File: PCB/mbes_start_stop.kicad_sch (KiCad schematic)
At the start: 15 parts, among them J1 IXTP3N50D2, Q10 BC817, Q12 BC817, Q16 BC817, Q17 BC327, Q18 BC327

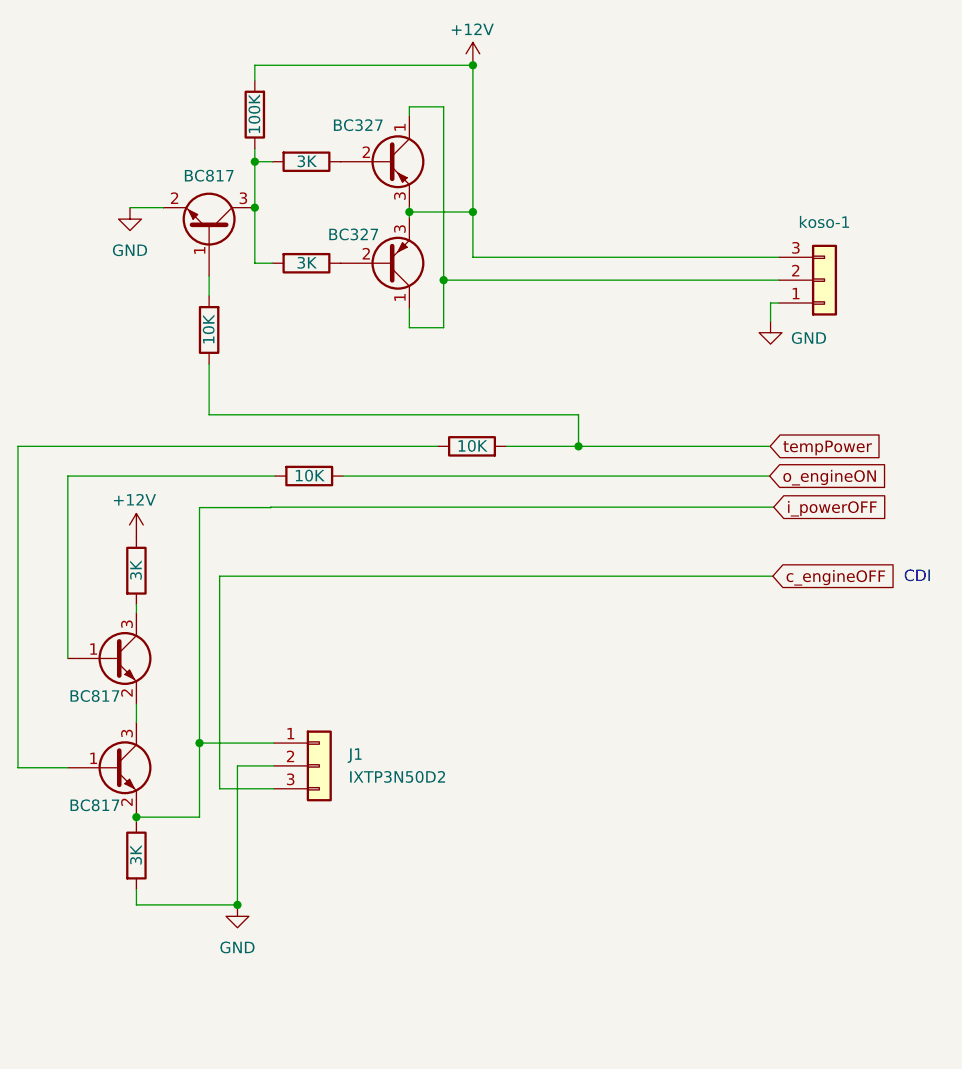
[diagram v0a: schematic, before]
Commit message: Engine-off mechanism
Deplation MOSfet has been substituted by a mechanical relay
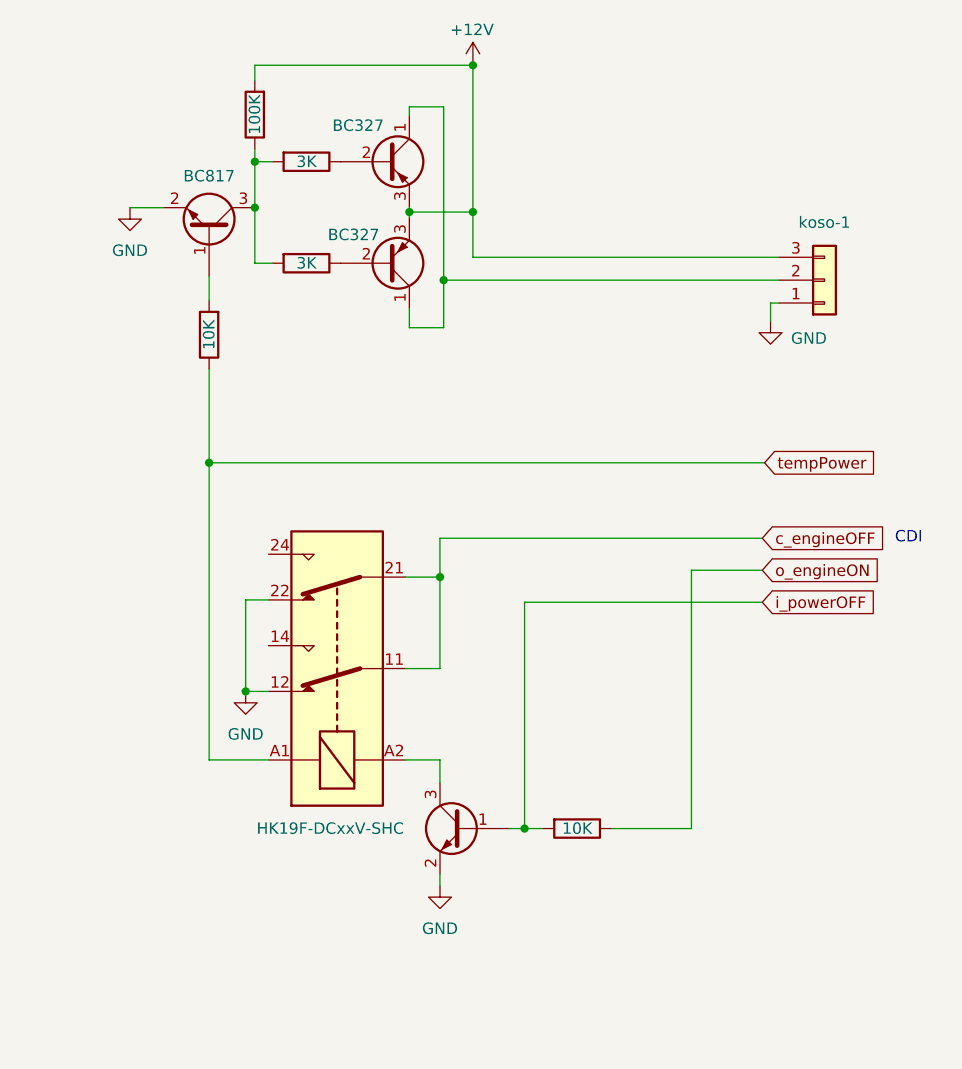
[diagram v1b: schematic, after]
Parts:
- removed J1: IXTP3N50D2, Connector_PinHeader_1.27mm:PinHeader_1x03_P1.27mm_Horizontal, symbol Connector_Generic:Conn_01x03
- removed Q16: BC817, Package_TO_SOT_SMD:SOT-23, symbol Transistor_BJT:BC817
- removed RA23: 10K, Resistor_SMD:R_1206_3216Metric, symbol Device:R
- removed RA29, RA43: 3K, Resistor_SMD:R_1206_3216Metric, symbol Device:R
- added K1: HK19F-DCxxV-SHC, Relay_THT:Relay_DPDT_Finder_30.22, symbol Relay:HK19F-DCxxV-SHC
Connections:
- net GND: now also Q12.2 (E), K1.12, K1.22
- net c_engineOFF: now also K1.11, K1.21
- net i_powerOFF: now also Q12.1 (B), RA44.2; no longer Q12.2 (E)
- net tempPower: now also K1.A1
- net at Q12.3 (C): now also K1.A2

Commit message: Wrong relay's power supply fixed
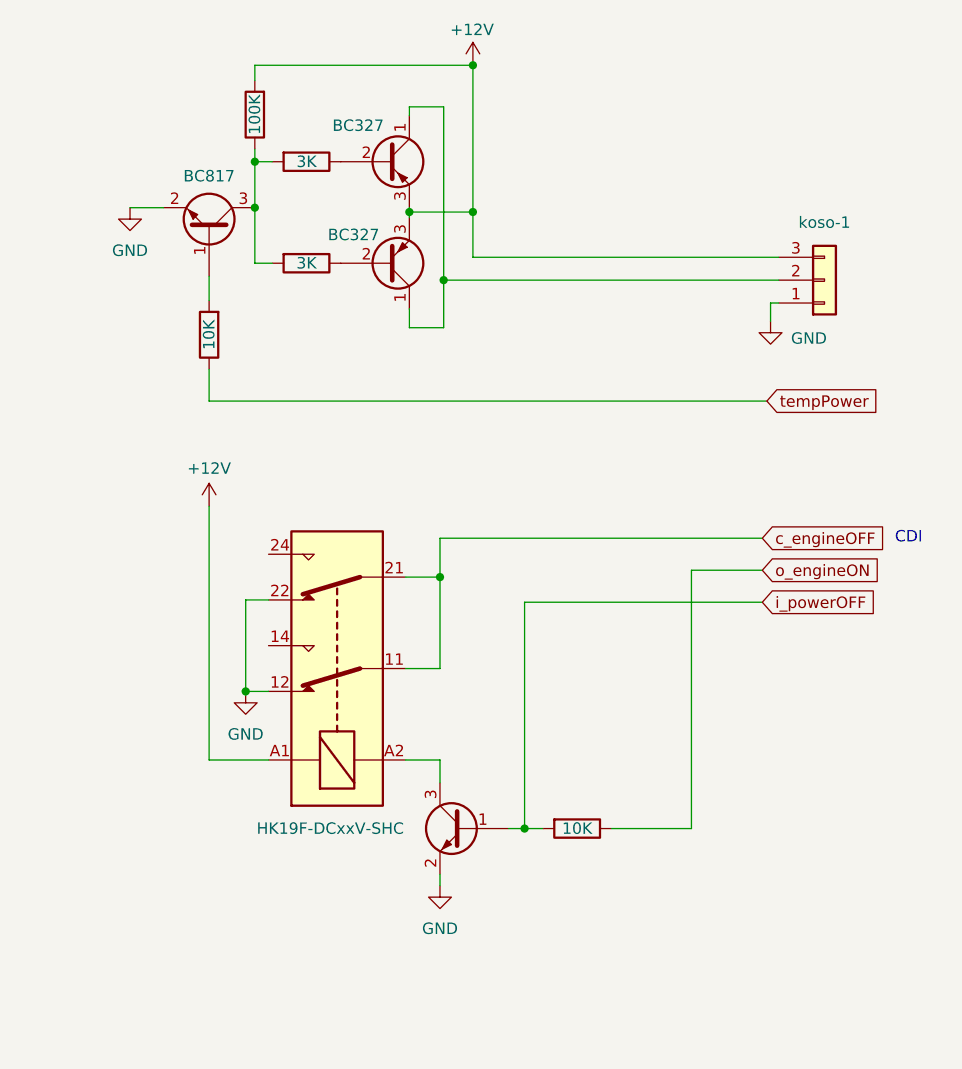
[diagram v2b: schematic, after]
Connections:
- net +12V: now also K1.A1
- net tempPower: no longer K1.A1
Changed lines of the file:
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@@
-	)
-	(junction
-		(at 89.916 121.92)
-		(diameter 0)
-		(color 0 0 0 0)
 	)
 	(junction
@@
 	(wire
 		(pts
-			(xy 89.916 111.506) (xy 89.916 121.92)
+			(xy 89.916 111.506) (xy 89.916 115.062)
 		)
 		(stroke
@@
 	(wire
 		(pts
+			(xy 89.916 126.746) (xy 89.916 154.94)
+		)
+		(stroke
+			(width 0)
+			(type default)
+		)
+	)
+	(wire
+		(pts
 			(xy 112.1664 94.0562) (xy 119.2276 94.0562)
 		)
@@
 	(wire
 		(pts
-			(xy 151.638 121.92) (xy 89.916 121.92)
+			(xy 151.892 115.062) (xy 89.916 115.062)
 		)
 		(stroke
@@
 		(pts
 			(xy 111.76 134.62) (xy 115.57 134.62)
-		)
-		(stroke
-			(width 0)
-			(type default)
-		)
-	)
-	(wire
-		(pts
-			(xy 89.916 121.92) (xy 89.916 154.94)
 		)
 		(stroke
@@
 	(global_label "tempPower"
 		(shape input)
-		(at 151.638 121.92 0)
+		(at 151.892 115.062 0)
 		(fields_autoplaced yes)
 		(effects
@@
 		)
 		(property "Intersheetrefs" "${INTERSHEET_REFS}"
-			(at 151.638 121.92 0)
+			(at 151.892 115.062 0)
 			(effects
 				(font
@@
 		)
 		(property "Riferimenti inter-foglio" "${INTERSHEET_REFS}"
-			(at 164.3321 121.8406 0)
+			(at 164.5861 114.9826 0)
 			(effects
 				(font
@@
 					(unit 1)
 				)
+			)
+		)
+	)
+	(symbol
+		(lib_id "power:+12V")
+		(at 89.916 126.746 0)
+		(unit 1)
+		(exclude_from_sim no)
+		(in_bom yes)
+		(on_board yes)
+		(dnp no)
+		(property "Reference" "#PWR04"
+			(at 89.916 130.556 0)
+			(effects
+				(font
+					(size 1.27 1.27)
+				)
+				(hide yes)
+			)
+		)
+		(property "Value" "+12V"
+			(at 89.916 122.555 0)
+			(effects
+				(font
+					(size 1.27 1.27)
+				)
+			)
+		)
+		(property "Footprint" ""
+			(at 89.916 126.746 0)
+			(effects
+				(font
+					(size 1.27 1.27)
+				)
+				(hide yes)
+			)
+		)
+		(property "Datasheet" ""
+			(at 89.916 126.746 0)
+			(effects
+				(font
+					(size 1.27 1.27)
+				)
+				(hide yes)
+			)
+		)
+		(property "Description" ""
+			(at 89.916 126.746 0)
+			(effects
+				(font
+					(size 1.27 1.27)
+				)
+				(hide yes)
+			)
+		)
+		(pin "1"
+		)
+		(instances
+			(project "pcb-b"
+				(path "/709d0967-afe5-49d3-92a5-d2bb94550bdb/58129762-4641-4cf0-a39a-a6f0d215df4c"
+					(reference "#PWR04")
+					(unit 1)
+				)

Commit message: More stable solution for BJT driving
The BJT-817 device's sensibility is very high. If you are doing some test and you weld a wire to che i_PowerOFF pin, then you
can find the transistor's sturation while the wire is not connected.
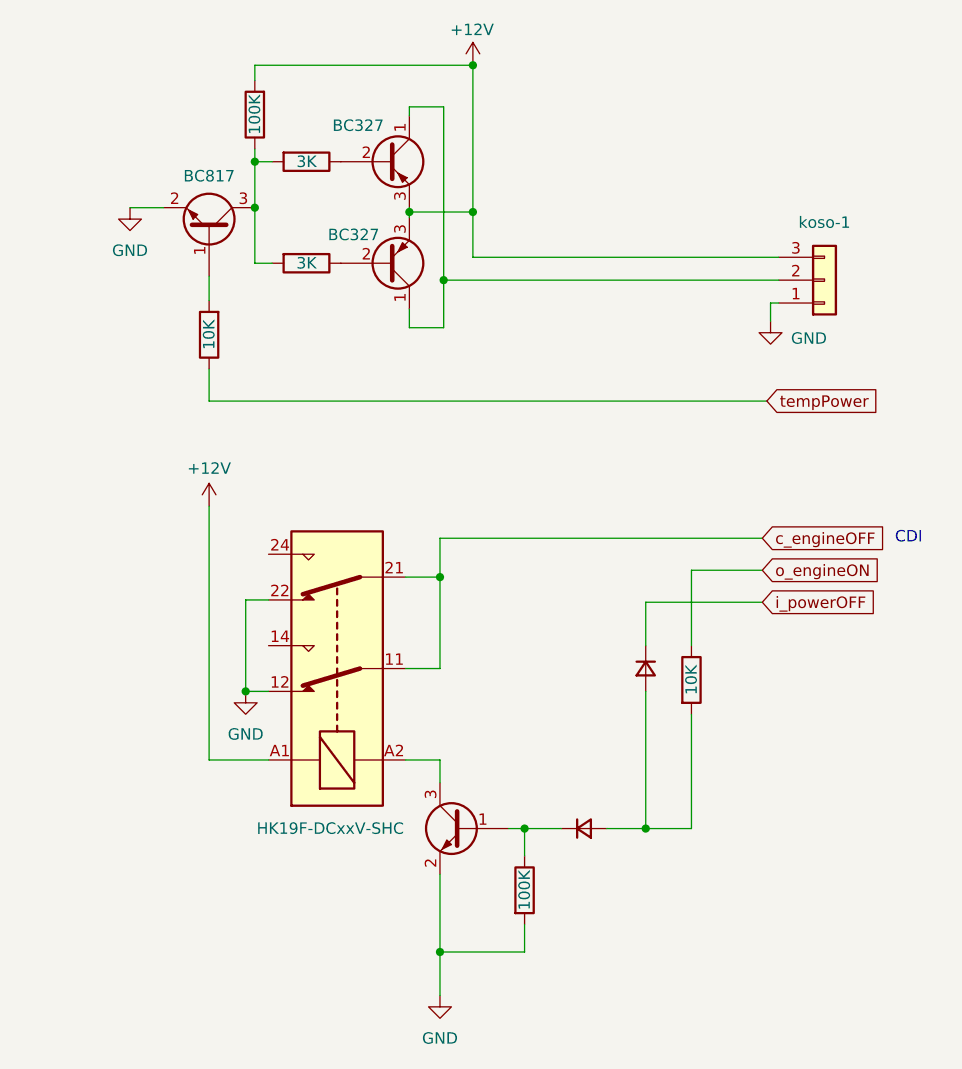
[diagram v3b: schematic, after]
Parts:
- added D2, D3: D_Small, Diode_SMD:D_1210_3225Metric_Pad1.42x2.65mm_HandSolder, symbol Device:D_Small
- added RA23: 100K, Resistor_SMD:R_1206_3216Metric, symbol Device:R
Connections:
- net GND: now also RA23.2
- net i_powerOFF: now also D2.1 (K); no longer Q12.1 (B), RA44.2
- new net: D2.2 (A), D3.2 (A), RA44.2
- new net: D3.1 (K), Q12.1 (B), RA23.1

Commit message: Important fixes and adjustments
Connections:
- no-connect marks 0 -> 2
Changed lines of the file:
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@@
 		(color 0 0 0 0)
+	)
+	(no_connect
+		(at 96.52 132.08)
+	)
+	(no_connect
+		(at 96.52 142.24)
 	)
 	(wire

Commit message: No USB support and PCB-B size reducing
Implementing USB power support using 7805 was a stupid idea: too much wasted electic current in Joule effect. So, I moved just
one 7805 in the PCB-A, because the its used power is very low. It allowed me to optimize the PCB-B used space and reduce its
whole size ;-)
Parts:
- removed D2, D3: D_Small, Diode_SMD:D_1210_3225Metric_Pad1.42x2.65mm_HandSolder, symbol Device:D_Small
- removed K1: HK19F-DCxxV-SHC, Relay_THT:Relay_DPDT_Finder_30.22, symbol Relay:HK19F-DCxxV-SHC
- removed Q10, Q12: BC817, Package_TO_SOT_SMD:SOT-23, symbol Transistor_BJT:BC817
- removed Q17, Q18: BC327, Package_TO_SOT_THT:TO-92L_Inline_Wide, symbol Transistor_BJT:BC327
- removed RA23, RA30: 100K, Resistor_SMD:R_1206_3216Metric, symbol Device:R
- removed RA31, RA33: 3K, Resistor_SMD:R_1206_3216Metric, symbol Device:R
- removed RA44, RA8: 10K, Resistor_SMD:R_1206_3216Metric, symbol Device:R
- removed koso-1: Conn_01x03, Connector_PinHeader_2.54mm:PinHeader_1x03_P2.54mm_Vertical, symbol Connector_Generic:Conn_01x03
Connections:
- no-connect marks 2 -> 0
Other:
- note removed: "CDI"
